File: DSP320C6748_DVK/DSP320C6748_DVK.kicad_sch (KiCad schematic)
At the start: 0 parts

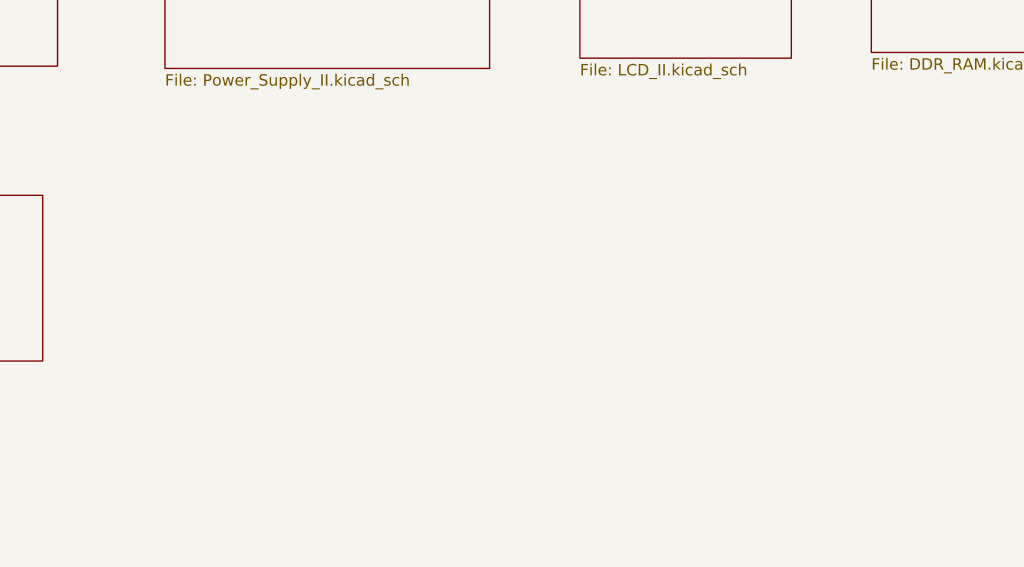
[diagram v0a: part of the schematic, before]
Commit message: Connectors and mislleneous components added
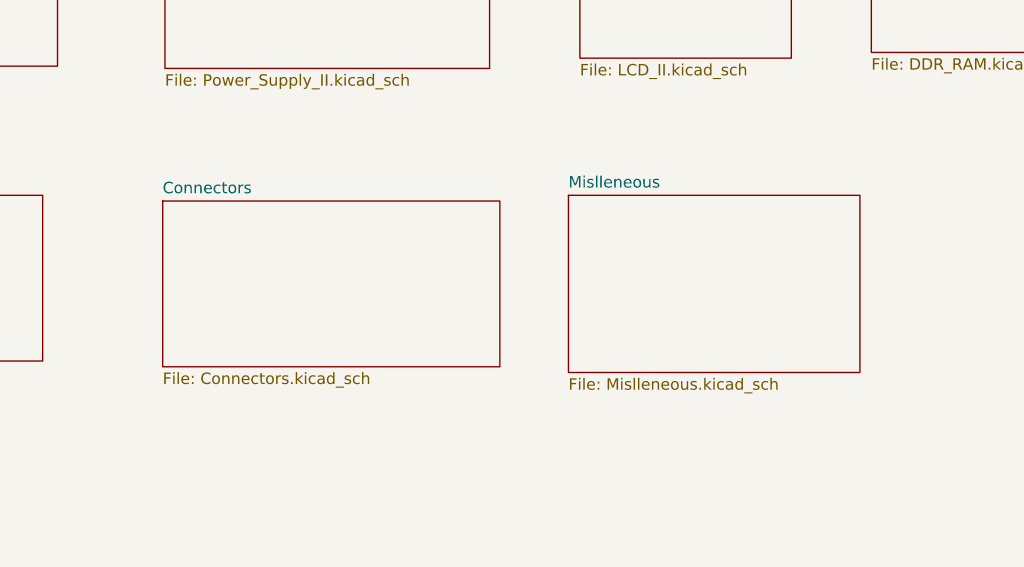
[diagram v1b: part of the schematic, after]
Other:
- added sheet Connectors (Connectors.kicad_sch)
- added sheet Mislleneous (Mislleneous.kicad_sch)
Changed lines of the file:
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@@
+	)
+	(sheet
+		(at 118.745 92.075)
+		(size 32.385 19.685)
+		(exclude_from_sim no)
+		(in_bom yes)
+		(on_board yes)
+		(dnp no)
+		(fields_autoplaced yes)
+		(stroke
+			(width 0.1524)
+			(type solid)
+		)
+		(fill
+			(color 0 0 0 0)
+		)
+		(property "Sheetname" "Mislleneous"
+			(at 118.745 91.3634 0)
+			(show_name no)
+			(do_not_autoplace no)
+			(effects
+				(font
+					(size 1.27 1.27)
+				)
+				(justify left bottom)
+			)
+		)
+		(property "Sheetfile" "Mislleneous.kicad_sch"
+			(at 118.745 112.3446 0)
+			(show_name no)
+			(do_not_autoplace no)
+			(effects
+				(font
+					(size 1.27 1.27)
+				)
+				(justify left top)
+			)
+		)
+		(instances
+			(project "DSP320C6748_DVK"
+				(path "/3a70ffc0-9fe7-4a5b-b3c2-23140355df82"
+					(page "16")
+				)
+			)
+		)
 	)
 	(sheet
@@
 				)
 			)
+		)
+	)
+	(sheet
+		(at 73.66 92.71)
+		(size 37.465 18.415)
+		(exclude_from_sim no)
+		(in_bom yes)
+		(on_board yes)
+		(dnp no)
+		(fields_autoplaced yes)
+		(stroke
+			(width 0.1524)
+			(type solid)
+		)
+		(fill
+			(color 0 0 0 0)
+		)
+		(property "Sheetname" "Connectors"
+			(at 73.66 91.9984 0)
+			(show_name no)
+			(do_not_autoplace no)
+			(effects
+				(font
+					(size 1.27 1.27)
+				)
+				(justify left bottom)
+			)
+		)
+		(property "Sheetfile" "Connectors.kicad_sch"
+			(at 73.66 111.7096 0)
+			(show_name no)
+			(do_not_autoplace no)
+			(effects
+				(font
+					(size 1.27 1.27)
+				)
+				(justify left top)
+			)
+		)
+		(instances
+			(project "DSP320C6748_DVK"
+				(path "/3a70ffc0-9fe7-4a5b-b3c2-23140355df82"
+					(page "15")
+				)
+			)

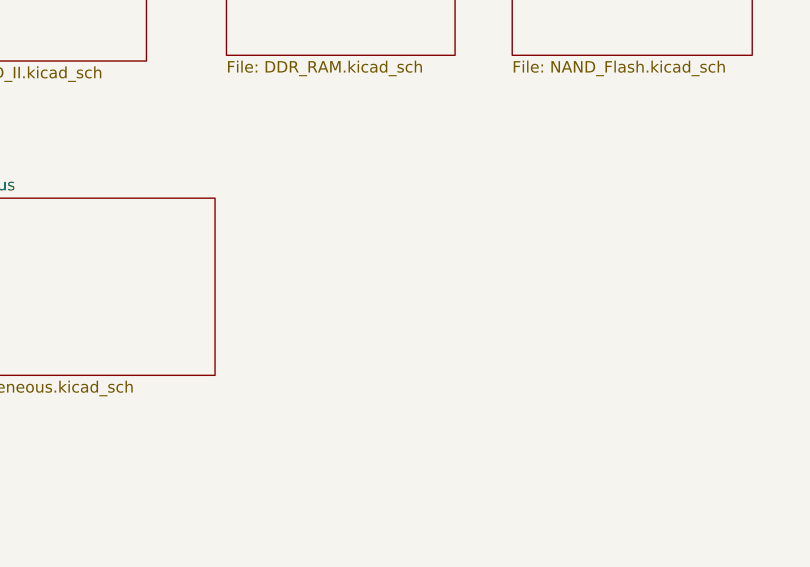
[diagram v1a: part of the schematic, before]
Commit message: DC jack Replaced With Type-C, ADC and RTC section added
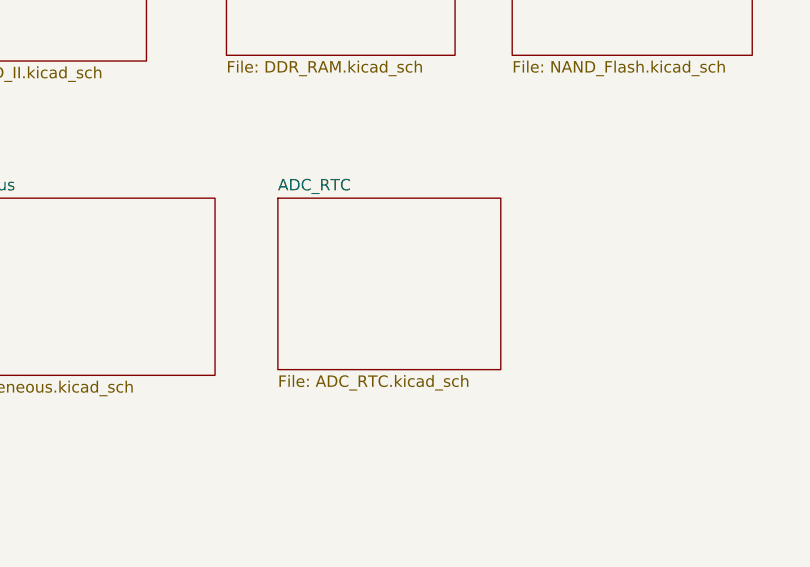
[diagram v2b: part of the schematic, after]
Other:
- added sheet ADC_RTC (ADC_RTC.kicad_sch)
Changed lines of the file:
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@@
+	)
+	(sheet
+		(at 158.115 92.075)
+		(size 24.765 19.05)
+		(exclude_from_sim no)
+		(in_bom yes)
+		(on_board yes)
+		(dnp no)
+		(fields_autoplaced yes)
+		(stroke
+			(width 0.1524)
+			(type solid)
+		)
+		(fill
+			(color 0 0 0 0)
+		)
+		(property "Sheetname" "ADC_RTC"
+			(at 158.115 91.3634 0)
+			(show_name no)
+			(do_not_autoplace no)
+			(effects
+				(font
+					(size 1.27 1.27)
+				)
+				(justify left bottom)
+			)
+		)
+		(property "Sheetfile" "ADC_RTC.kicad_sch"
+			(at 158.115 111.7096 0)
+			(show_name no)
+			(do_not_autoplace no)
+			(effects
+				(font
+					(size 1.27 1.27)
+				)
+				(justify left top)
+			)
+		)
+		(instances
+			(project "DSP320C6748_DVK"
+				(path "/3a70ffc0-9fe7-4a5b-b3c2-23140355df82"
+					(page "17")
+				)
+			)
+		)
 	)
 	(sheet
